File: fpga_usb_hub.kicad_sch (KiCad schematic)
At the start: 146 parts, among them SW1.RST? 1-1825027-1, SW2.OSD? 1-1825027-1, SW3.USR? 1-1825027-1

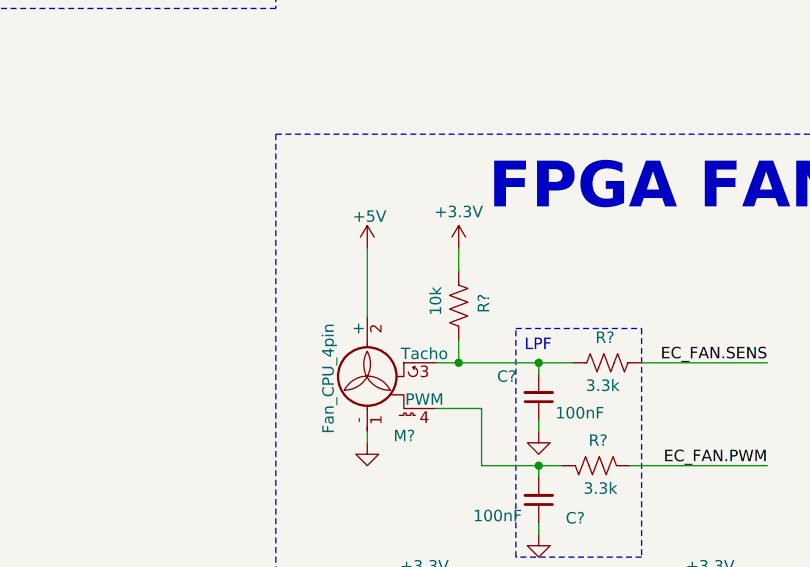
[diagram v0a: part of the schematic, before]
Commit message: Option to power the FAN with USB-C Supply directly.
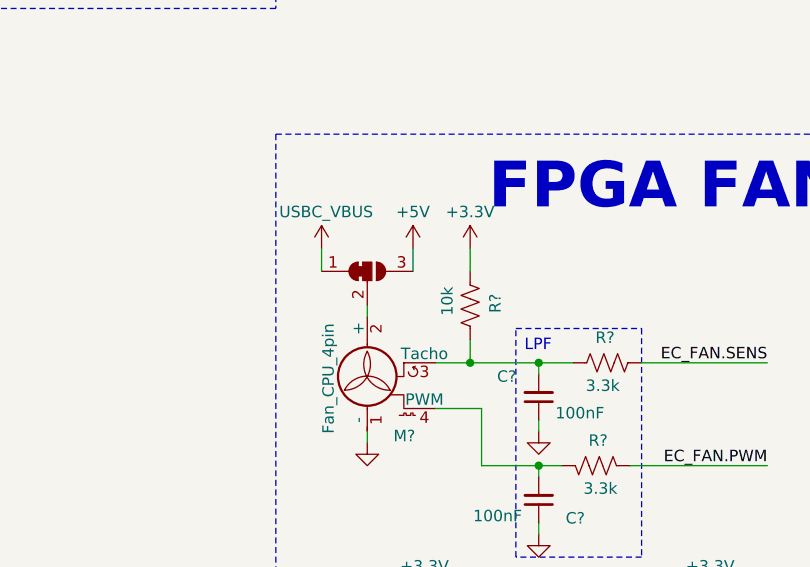
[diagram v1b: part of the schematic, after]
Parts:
- added JP1: SolderJumper_3_Bridged12, Jumper:SolderJumper-3_P1.3mm_Bridged12_RoundedPad1.0x1.5mm, symbol Jumper:SolderJumper_3_Bridged12
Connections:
- net +5V: now also JP1.3 (B); no longer M?.2 (+)
- net USBC_VBUS: now also JP1.1 (A)
- new net: JP1.2 (C), M?.2 (+)
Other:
- moved on the sheet: R?
